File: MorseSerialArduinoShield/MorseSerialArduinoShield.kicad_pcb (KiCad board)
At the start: 2 copper layers, 76.2 x 54.6 mm, 13 parts, among them J1 HC_05, U1 SC39-11SRWA

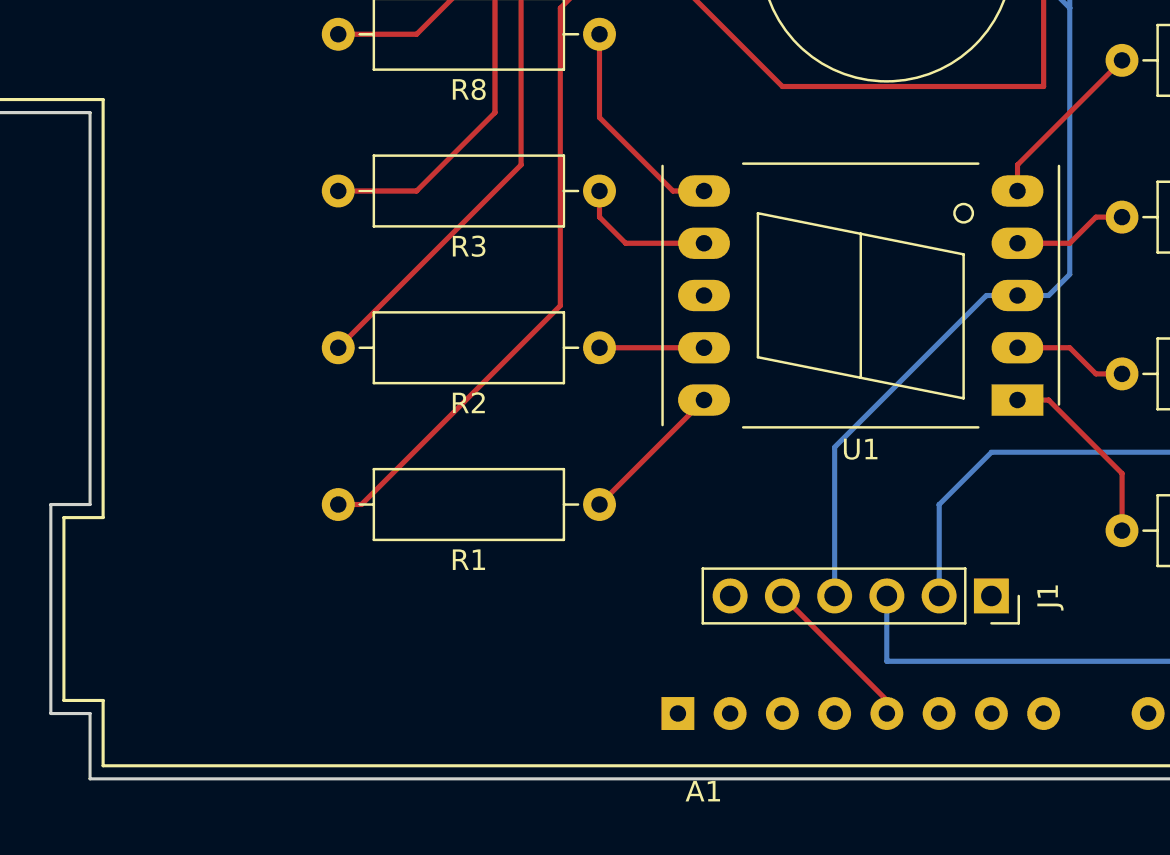
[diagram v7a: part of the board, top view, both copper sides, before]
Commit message: Added external power pins for a battery and added JLC marker for production when ready
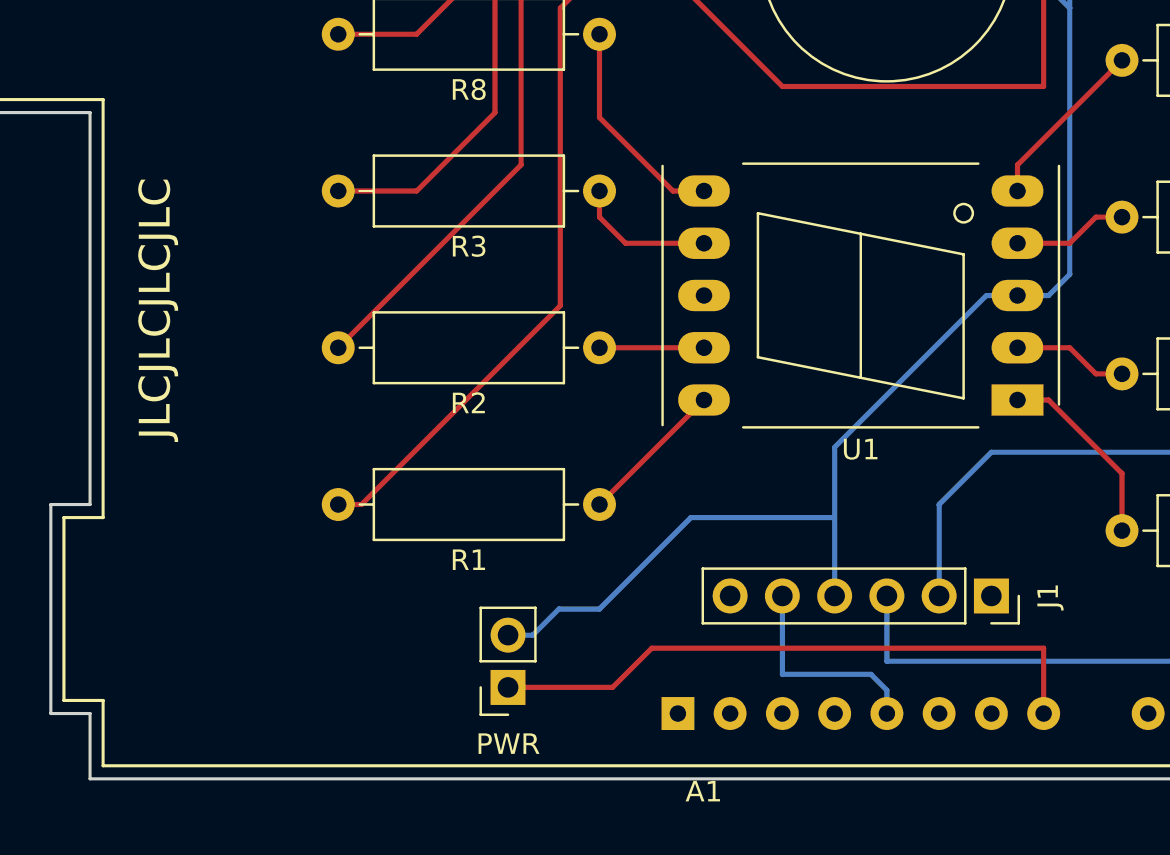
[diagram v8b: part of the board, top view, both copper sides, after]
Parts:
- added PWR: PWR and GND, Connector_PinSocket_2.54mm:PinSocket_1x02_P2.54mm_Vertical, F.Cu at (130.7, 125.1)
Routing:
- net Net-(A1-Pad8): track 0.00 -> 30.0 mm
- net GND: track 74.9 -> 93.2 mm
- net Net-(A1-Pad5): track 7.82 -> 10.3 mm
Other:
- board text added: "JLCJLCJLCJLC"
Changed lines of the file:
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@@
   (general
     (thickness 1.6)
-    (drawings 38)
-    (tracks 93)
+    (drawings 39)
+    (tracks 104)
     (zones 0)
-    (modules 13)
+    (modules 14)
     (nets 45)
   )
@@
     (add_net "Net-(R8-Pad1)")
     (add_net "Net-(U1-Pad8)")
+  )
+  (module Connector_PinSocket_2.54mm:PinSocket_1x02_P2.54mm_Vertical (layer F.Cu)
+    (at 130.683 125.095 180)
+    (descr "Through hole straight socket strip, 1x02, 2.54mm pitch, single row (from Kicad 4.0.7), script generated")
+    (tags "Through hole socket strip THT 1x02 2.54mm single row")
+    (fp_text reference PWR (at 0 -2.77) (layer F.SilkS)
+      (effects (font (size 1 1) (thickness 0.15)))
+    )
+    (fp_text value "PWR and GND" (at 0 5.31) (layer F.Fab)
+      (effects (font (size 1 1) (thickness 0.15)))
+    )
+    (fp_text user %R (at 0 1.27 90) (layer F.Fab)
+      (effects (font (size 1 1) (thickness 0.15)))
+    )
+    (fp_line (start -1.8 4.3) (end -1.8 -1.8) (layer F.CrtYd) (width 0.05))
+    (fp_line (start 1.75 4.3) (end -1.8 4.3) (layer F.CrtYd) (width 0.05))
+    (fp_line (start 1.75 -1.8) (end 1.75 4.3) (layer F.CrtYd) (width 0.05))
+    (fp_line (start -1.8 -1.8) (end 1.75 -1.8) (layer F.CrtYd) (width 0.05))
+    (fp_line (start 0 -1.33) (end 1.33 -1.33) (layer F.SilkS) (width 0.12))
+    (fp_line (start 1.33 -1.33) (end 1.33 0) (layer F.SilkS) (width 0.12))
+    (fp_line (start 1.33 1.27) (end 1.33 3.87) (layer F.SilkS) (width 0.12))
+    (fp_line (start -1.33 3.87) (end 1.33 3.87) (layer F.SilkS) (width 0.12))
+    (fp_line (start -1.33 1.27) (end -1.33 3.87) (layer F.SilkS) (width 0.12))
+    (fp_line (start -1.33 1.27) (end 1.33 1.27) (layer F.SilkS) (width 0.12))
+    (fp_line (start -1.27 3.81) (end -1.27 -1.27) (layer F.Fab) (width 0.1))
+    (fp_line (start 1.27 3.81) (end -1.27 3.81) (layer F.Fab) (width 0.1))
+    (fp_line (start 1.27 -0.635) (end 1.27 3.81) (layer F.Fab) (width 0.1))
+    (fp_line (start 0.635 -1.27) (end 1.27 -0.635) (layer F.Fab) (width 0.1))
+    (fp_line (start -1.27 -1.27) (end 0.635 -1.27) (layer F.Fab) (width 0.1))
+    (pad 2 thru_hole oval (at 0 2.54 180) (size 1.7 1.7) (drill 1) (layers *.Cu *.Mask)
+      (net 1 GND))
+    (pad 1 thru_hole rect (at 0 0 180) (size 1.7 1.7) (drill 1) (layers *.Cu *.Mask)
+      (net 16 "Net-(A1-Pad8)"))
+    (model ${KISYS3DMOD}/Connector_PinSocket_2.54mm.3dshapes/PinSocket_1x02_P2.54mm_Vertical.wrl
+      (at (xyz 0 0 0))
+      (scale (xyz 1 1 1))
+      (rotate (xyz 0 0 0))
+    )
   )
   (module Connector_PinSocket_2.54mm:PinSocket_1x06_P2.54mm_Vertical (layer F.Cu)
@@
     )
   )
+  (gr_text JLCJLCJLCJLC (at 113.538 106.68 90) (layer F.SilkS)
+    (effects (font (size 1.5 1.5) (thickness 0.3)))
+  )
   (gr_line (start 110.363 74.93) (end 110.998 74.93) (layer Edge.Cuts) (width 0.15))
   (gr_line (start 110.363 84.455) (end 110.363 74.93) (layer Edge.Cuts) (width 0.15))
@@
   (segment (start 146.558 113.423) (end 153.936 106.045) (width 0.25) (layer B.Cu) (net 1))
   (segment (start 146.558 120.65) (end 146.558 113.423) (width 0.25) (layer B.Cu) (net 1))
+  (segment (start 131.885081 122.555) (end 133.155081 121.285) (width 0.25) (layer B.Cu) (net 1))
+  (segment (start 130.683 122.555) (end 131.885081 122.555) (width 0.25) (layer B.Cu) (net 1))
+  (segment (start 133.155081 121.285) (end 135.128 121.285) (width 0.25) (layer B.Cu) (net 1))
+  (segment (start 135.128 121.285) (end 139.573 116.84) (width 0.25) (layer B.Cu) (net 1))
+  (segment (start 139.573 116.84) (end 146.558 116.84) (width 0.25) (layer B.Cu) (net 1))
   (segment (start 171.958 80.01) (end 171.958 78.105) (width 0.25) (layer B.Cu) (net 2))
   (segment (start 151.638 116.205) (end 154.178 113.665) (width 0.25) (layer B.Cu) (net 2))
@@
   (segment (start 137.418 88.265) (end 147.578 78.105) (width 0.25) (layer F.Cu) (net 13))
   (segment (start 133.22159 88.265) (end 137.418 88.265) (width 0.25) (layer F.Cu) (net 13))
+  (segment (start 135.763 125.095) (end 130.683 125.095) (width 0.25) (layer F.Cu) (net 16))
+  (segment (start 137.668 123.19) (end 135.763 125.095) (width 0.25) (layer F.Cu) (net 16))
+  (segment (start 156.718 126.365) (end 156.718 123.19) (width 0.25) (layer F.Cu) (net 16))
+  (segment (start 156.718 123.19) (end 137.668 123.19) (width 0.25) (layer F.Cu) (net 16))
   (segment (start 122.428 108.585) (end 131.318 99.695) (width 0.25) (layer F.Cu) (net 17))
   (segment (start 131.318 99.695) (end 131.318 90.805) (width 0.25) (layer F.Cu) (net 17))
@@
   (segment (start 163.068 81.915) (end 159.258 78.105) (width 0.25) (layer F.Cu) (net 21))
   (segment (start 163.068 99.695) (end 163.068 81.915) (width 0.25) (layer F.Cu) (net 21))
-  (segment (start 149.098 125.73) (end 149.098 126.365) (width 0.25) (layer F.Cu) (net 22))
-  (segment (start 144.018 120.65) (end 149.098 125.73) (width 0.25) (layer F.Cu) (net 22))
+  (segment (start 148.32437 124.46) (end 144.018 124.46) (width 0.25) (layer B.Cu) (net 22))
+  (segment (start 144.018 124.46) (end 144.018 120.65) (width 0.25) (layer B.Cu) (net 22))
+  (segment (start 149.098 126.365) (end 149.098 125.23363) (width 0.25) (layer B.Cu) (net 22))
+  (segment (start 149.098 125.23363) (end 148.32437 124.46) (width 0.25) (layer B.Cu) (net 22))
   (segment (start 173.228 117.475) (end 175.768 114.935) (width 0.25) (layer F.Cu) (net 23))
   (segment (start 175.768 114.935) (end 175.768 108.585) (width 0.25) (layer F.Cu) (net 23))
